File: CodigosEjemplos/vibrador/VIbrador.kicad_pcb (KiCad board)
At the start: 2 copper layers, 5 parts, among them U2 ArduinoNANO, U3 Buzzer, U4 HC-05, U5 Buzzer

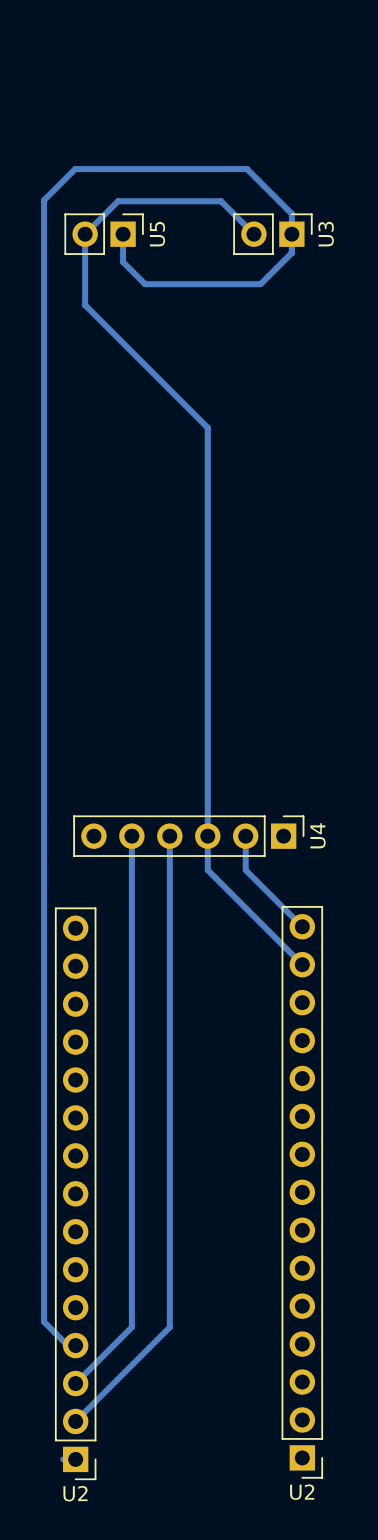
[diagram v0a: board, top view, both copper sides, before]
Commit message: Se agregó zona de relleno
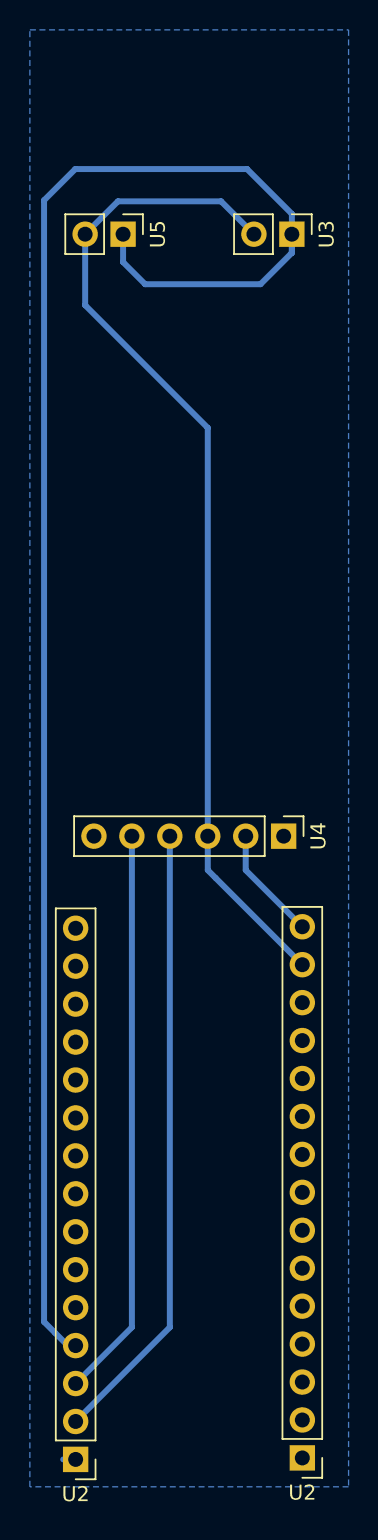
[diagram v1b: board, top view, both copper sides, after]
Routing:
- added copper zone on B.Cu, net GND
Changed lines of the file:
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@@
   )
   (setup
-    (last_trace_width 0.4)
+    (last_trace_width 0.25)
     (user_trace_width 0.4)
     (trace_clearance 0.2)
@@
   (segment (start 95.476 154.675999) (end 95.476 121.796) (width 0.4) (layer B.Cu) (net 5))
   (segment (start 91.711 158.440999) (end 95.476 154.675999) (width 0.4) (layer B.Cu) (net 5))
+  (zone (net 2) (net_name GND) (layer B.Cu) (hatch edge 0.508)
+    (connect_pads (clearance 0.508))
+    (min_thickness 0.254)
+    (fill yes (arc_segments 32) (thermal_gap 0.508) (thermal_bridge_width 0.508))
+    (polygon
+      (pts
+        (xy 109.982 165.354) (xy 88.646 165.354) (xy 88.646 67.818) (xy 109.982 67.818)
+      )
+    )
+  )
 )

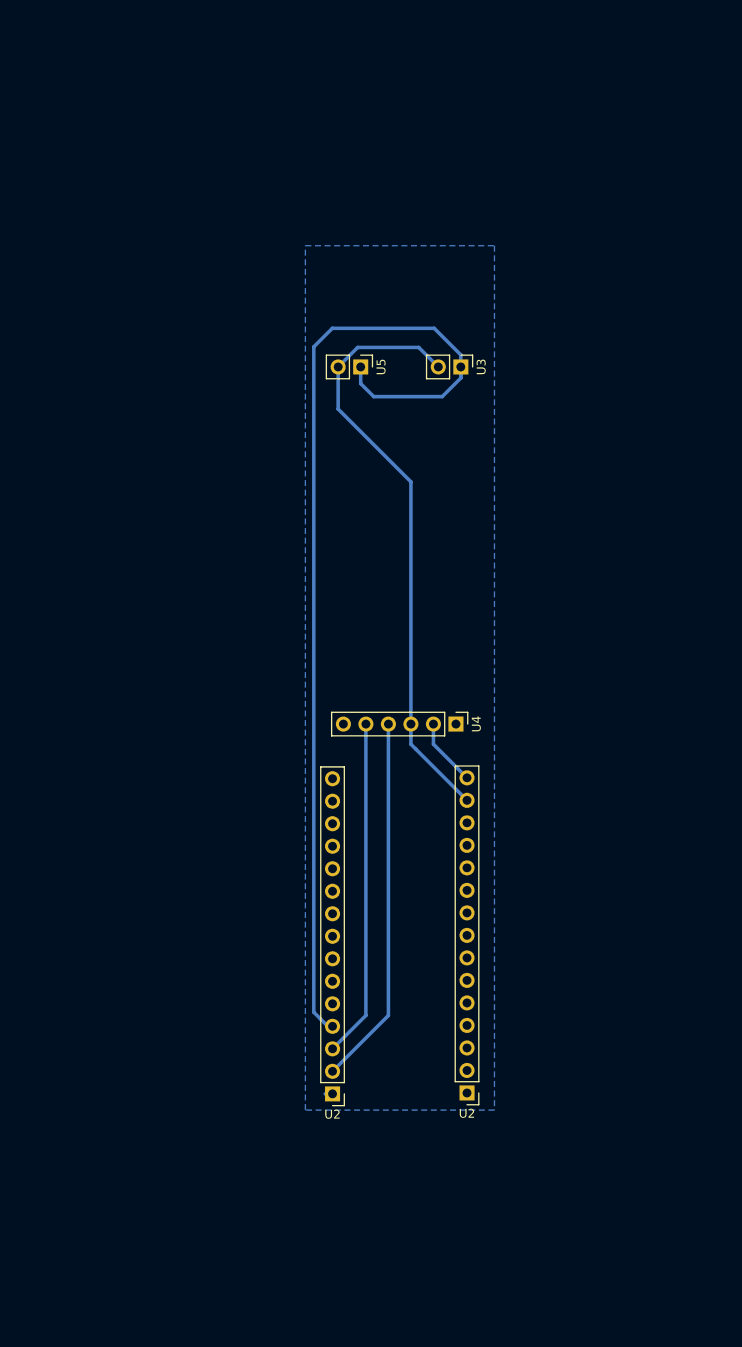
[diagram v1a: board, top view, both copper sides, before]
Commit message: Se agregaron los PCB de HC-05, pila (falta completar) y vibrador
Tambien cambie el simbolo de hc-05 ya que le faltaban dos pines
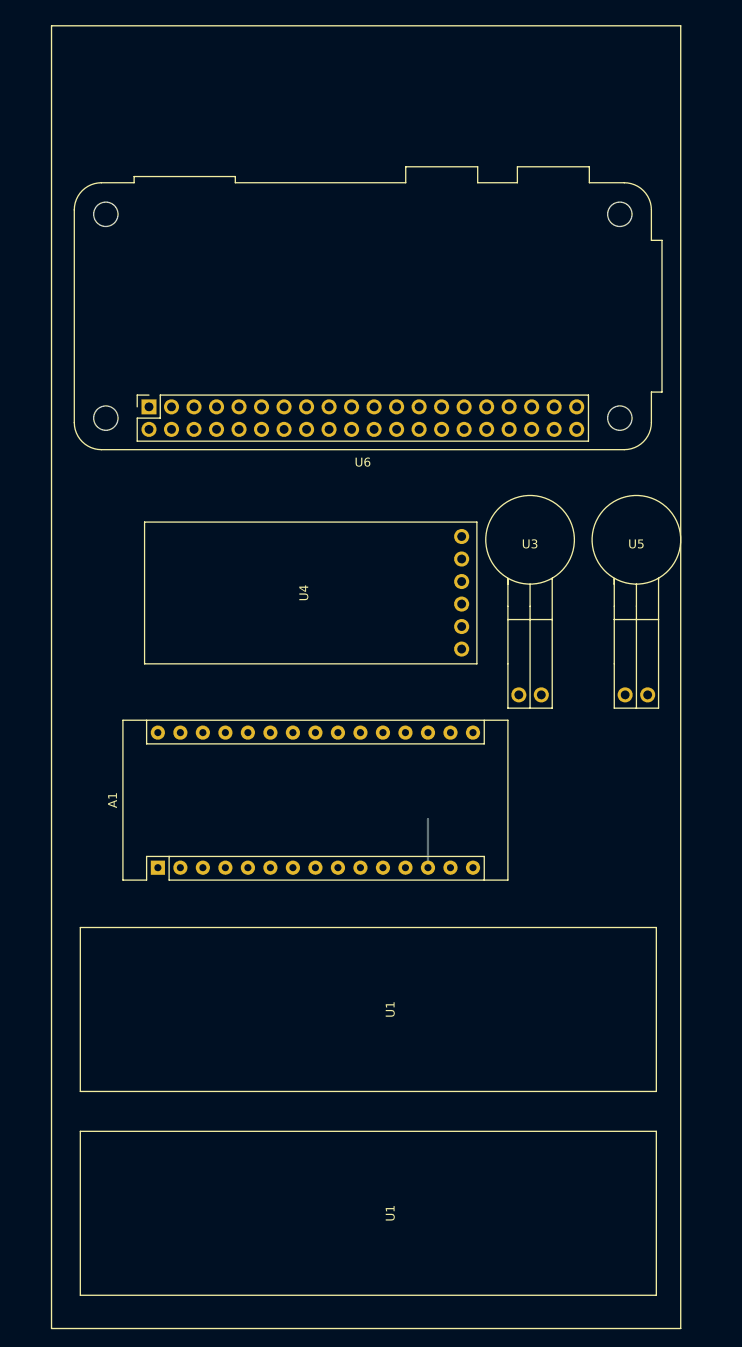
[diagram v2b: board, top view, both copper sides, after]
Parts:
- removed U2 (x2): ArduinoNANO, Connector_PinHeader_2.54mm:PinHeader_1x15_P2.54mm_Vertical
- added A1: Arduino_Nano_v3.x, Module:Arduino_Nano, F.Cu at (72.0, 138.0)
- added U1: Pila3,7V, VibradorPCB:Pila de Litio, F.Cu at (130.0, 154.0)
- added U1: Pila3,7V, VibradorPCB:Pila de Litio, F.Cu at (130.0, 177.0)
- added U6: PiZeroW, Module:Raspberry_Pi_Zero_Socketed_THT_FaceDown_MountingHoles, F.Cu at (71.0, 86.0)
- U3, U5: footprint Connector_PinHeader_2.54mm:PinHeader_1x02_P2.54mm_Vertical -> VibradorPCB:Vibrador
- U4: footprint Connector_PinHeader_2.54mm:PinHeader_1x06_P2.54mm_Vertical -> VibradorPCB:HC-05
- moved U5 36.7 mm to (126.0, 101.0), turned to 0 degrees
- moved U3 21.0 mm to (114.0, 101.0), turned to 0 degrees
- moved U4 15.2 mm to (109.0, 107.0), turned to 90 degrees
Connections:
- U4 pad 1: (no net) -> Net-(U4-Pad1)
- U4 pad 6: (no net) -> Net-(U4-Pad6)
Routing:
- net D9: track 114.5 -> 0.00 mm
- net GND: track 68.1 -> 0.00 mm
- net RX: track 41.8 -> 0.00 mm
- net TX: track 38.2 -> 5.48 mm
- net VIN: track 7.63 -> 0.00 mm
- removed copper zone on B.Cu, net GND

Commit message: Se actualizo la poscion de la raspberry para conveniencia de la pi camera
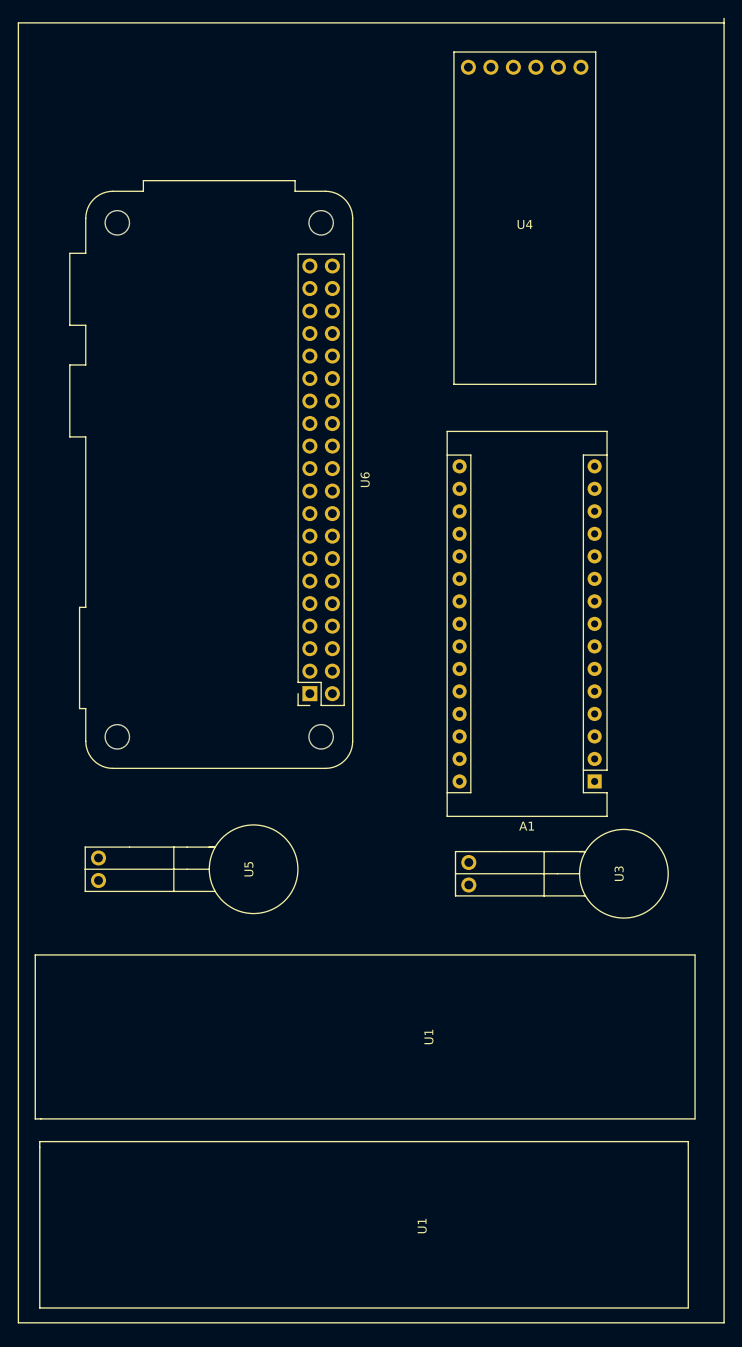
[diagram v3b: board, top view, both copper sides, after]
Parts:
- moved U4 62.2 mm to (113.4, 45.0), turned to 180 degrees
- moved U5 57.0 mm to (82.8, 138.2), turned to 270 degrees
- moved A1 50.2 mm to (121.3, 128.3), turned to 180 degrees
- moved U3 39.1 mm to (124.6, 138.7), turned to 270 degrees
- moved U6 37.1 mm to (89.2, 118.4), turned to 180 degrees
- moved U1 5.35 mm to (134.4, 157.1)
- moved U1 3.88 mm to (133.6, 178.4)
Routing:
- net TX: track 5.48 -> 0.00 mm

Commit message: PCB con StepDown
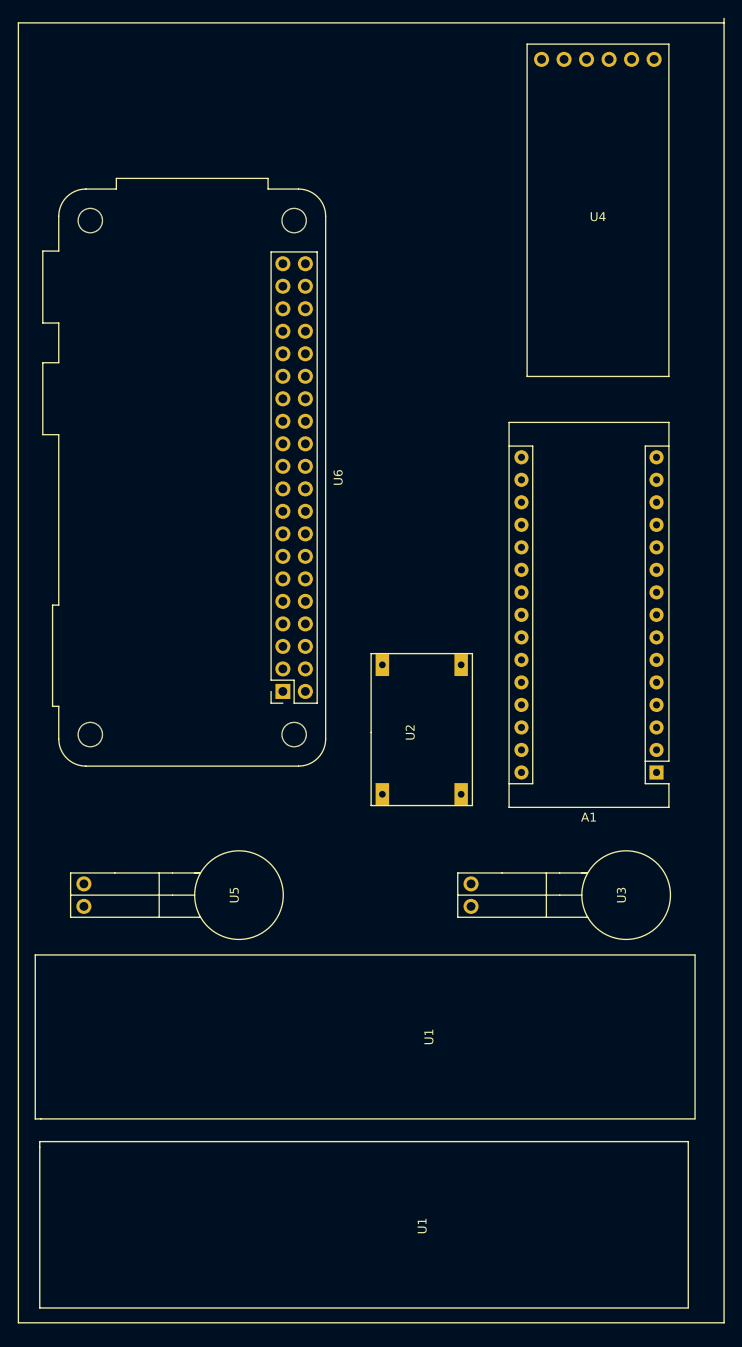
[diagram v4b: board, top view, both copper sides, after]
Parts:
- added U2: StepDown, VibradorPCB:StepDown, F.Cu at (96.1, 122.7)
- moved U4 8.30 mm to (121.7, 44.1)
- moved A1 7.06 mm to (128.3, 127.3)
- moved U5 3.36 mm to (81.2, 141.1)
- moved U6 3.06 mm to (86.1, 118.1)
- moved U3 2.43 mm to (124.8, 141.1)
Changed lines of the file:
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@@
     (tracks 0)
     (zones 0)
-    (modules 7)
-    (nets 72)
+    (modules 8)
+    (nets 76)
   )
   (page A4 portrait)
@@
   (net 70 "Net-(A1-Pad17)")
   (net 71 "Net-(A1-Pad1)")
+  (net 72 IN+)
+  (net 73 OUT+)
+  (net 74 IN-)
+  (net 75 OUT-)
   (net_class Default "Esta es la clase de red por defecto."
     (clearance 0.2)
@@
     (add_net D9)
     (add_net GND)
+    (add_net IN+)
+    (add_net IN-)
     (add_net "Net-(A1-Pad1)")
     (add_net "Net-(A1-Pad10)")
@@
     (add_net "Net-(U6-Pad8)")
     (add_net "Net-(U6-Pad9)")
+    (add_net OUT+)
+    (add_net OUT-)
     (add_net RX)
     (add_net TX)
     (add_net VIN)
-  )
-  (module "VibradorPCB:Pila de Litio" (layer F.Cu)
-    (at 134.366 157.099 90)
-    (fp_text reference U1 (at 0 -31.75 90) (layer F.SilkS)
-      (effects (font (size 1 1) (thickness 0.15)))
-    )
-    (fp_text value Pila3,7V (at 0 -28.75 90) (layer F.Fab)
-      (effects (font (size 1 1) (thickness 0.15)))
-    )
-    (fp_line (start -9.25 -1.75) (end 9.25 -1.75) (layer F.SilkS) (width 0.12))
-    (fp_line (start 9.25 -1.75) (end 9.25 -76.2) (layer F.SilkS) (width 0.15))
-    (fp_line (start -9.25 -1.75) (end -9.25 -75.565) (layer F.SilkS) (width 0.15))
-    (fp_line (start 9.25 -76.2) (end -9.25 -76.2) (layer F.SilkS) (width 0.15))
-    (fp_line (start -9.25 -75.565) (end -9.25 -76.2) (layer F.SilkS) (width 0.15))
   )
   (module "VibradorPCB:Pila de Litio" (layer F.Cu)
@@
     (fp_line (start 9.525 -74.93) (end 8.89 -74.93) (layer F.SilkS) (width 0.15))
   )
+  (module "VibradorPCB:Pila de Litio" (layer F.Cu)
+    (at 134.366 157.099 90)
+    (fp_text reference U1 (at 0 -31.75 90) (layer F.SilkS)
+      (effects (font (size 1 1) (thickness 0.15)))
+    )
+    (fp_text value Pila3,7V (at 0 -28.75 90) (layer F.Fab)
+      (effects (font (size 1 1) (thickness 0.15)))
+    )
+    (fp_line (start -9.25 -1.75) (end 9.25 -1.75) (layer F.SilkS) (width 0.12))
+    (fp_line (start 9.25 -1.75) (end 9.25 -76.2) (layer F.SilkS) (width 0.15))
+    (fp_line (start -9.25 -1.75) (end -9.25 -75.565) (layer F.SilkS) (width 0.15))
+    (fp_line (start 9.25 -76.2) (end -9.25 -76.2) (layer F.SilkS) (width 0.15))
+    (fp_line (start -9.25 -75.565) (end -9.25 -76.2) (layer F.SilkS) (width 0.15))
+  )
   (module Module:Raspberry_Pi_Zero_Socketed_THT_FaceDown_MountingHoles (layer F.Cu)
-    (at 89.154 118.364 180)
+    (at 86.106 118.11 180)
     (descr "Raspberry Pi Zero using through hole straight pin socket, 2x20, 2.54mm pitch, https://www.raspberrypi.org/documentation/hardware/raspberrypi/mechanical/rpi_MECH_Zero_1p2.pdf")
     (tags "raspberry pi zero through hole")
@@
   )
   (module Module:Arduino_Nano (layer F.Cu)
-    (at 121.285 128.27 180)
+    (at 128.27 127.254 180)
     (descr "Arduino Nano, http://www.mouser.com/pdfdocs/Gravitech_Arduino_Nano3_0.pdf")
     (tags "Arduino Nano")
@@
   )
   (module VibradorPCB:HC-05 (layer F.Cu)
-    (at 113.411 44.958 180)
+    (at 121.666 44.069 180)
     (fp_text reference U4 (at 0 -20.5) (layer F.SilkS)
       (effects (font (size 1 1) (thickness 0.15)))
@@
   )
   (module VibradorPCB:Vibrador (layer F.Cu)
-    (at 124.587 138.684 270)
+    (at 124.841 141.097 270)
     (fp_text reference U3 (at 0 0.5 90) (layer F.SilkS)
       (effects (font (size 1 1) (thickness 0.15)))
@@
   )
   (module VibradorPCB:Vibrador (layer F.Cu)
-    (at 82.804 138.176 270)
+    (at 81.153 141.097 270)
     (fp_text reference U5 (at 0 0.5 90) (layer F.SilkS)
       (effects (font (size 1 1) (thickness 0.15)))
@@
       (net 1 D9))
   )
+  (module VibradorPCB:StepDown (layer F.Cu)
+    (at 96.0628 122.7328 90)
+    (fp_text reference U2 (at 0 4.445 90) (layer F.SilkS)
+      (effects (font (size 1 1) (thickness 0.15)))
+    )
+    (fp_text value StepDown (at 0 6.35 90) (layer F.Fab)
+      (effects (font (size 1 1) (thickness 0.15)))
+    )
+    (fp_line (start 0 0) (end 8.89 0) (layer F.SilkS) (width 0.15))
+    (fp_line (start 8.89 0) (end 8.89 11.43) (layer F.SilkS) (width 0.15))
+    (fp_line (start 8.89 11.43) (end -8.255 11.43) (layer F.SilkS) (width 0.15))
+    (fp_line (start -8.255 11.43) (end -8.255 0) (layer F.SilkS) (width 0.15))
+    (fp_line (start -8.255 0) (end 0 0) (layer F.SilkS) (width 0.15))
+    (pad 1 thru_hole rect (at -6.985 1.27 90) (size 2.524 1.524) (drill 0.762) (layers *.Cu *.Mask)
+      (net 72 IN+))
+    (pad 2 thru_hole rect (at 7.62 1.27 90) (size 2.524 1.524) (drill 0.762) (layers *.Cu *.Mask)
+      (net 73 OUT+))
+    (pad 3 thru_hole rect (at -6.985 10.16 90) (size 2.524 1.524) (drill 0.762) (layers *.Cu *.Mask)
+      (net 74 IN-))
+    (pad 4 thru_hole rect (at 7.62 10.16 90) (size 2.524 1.524) (drill 0.762) (layers *.Cu *.Mask)
+      (net 75 OUT-))
+  )
   (gr_line (start 56.261 42.672) (end 135.89 42.672) (layer F.SilkS) (width 0.15))
